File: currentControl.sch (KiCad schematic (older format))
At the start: 5 parts

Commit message: updated with association labels
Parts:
- gave numbers to parts that had none: 5
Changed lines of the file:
@@
 $EndDescr
 $Comp
-L GND #PWR?
+L GND #PWR205
 U 1 1 5521A09C
 P 5100 4750
-F 0 "#PWR?" H 5100 4500 60  0001 C CNN
+F 0 "#PWR205" H 5100 4500 60  0001 C CNN
 F 1 "GND" H 5100 4600 60  0000 C CNN
 F 2 "" H 5100 4750 60  0000 C CNN
@@
 $EndComp
 $Comp
-L GND #PWR?
+L GND #PWR201
 U 1 1 5521A0A9
 P 4300 3850
-F 0 "#PWR?" H 4300 3600 60  0001 C CNN
+F 0 "#PWR201" H 4300 3600 60  0001 C CNN
 F 1 "GND" H 4300 3700 60  0000 C CNN
 F 2 "" H 4300 3850 60  0000 C CNN
@@
 $EndComp
 $Comp
-L GND #PWR?
+L GND #PWR206
 U 1 1 5521A0D3
 P 5100 4750
-F 0 "#PWR?" H 5100 4500 60  0001 C CNN
+F 0 "#PWR206" H 5100 4500 60  0001 C CNN
 F 1 "GND" H 5100 4600 60  0000 C CNN
 F 2 "" H 5100 4750 60  0000 C CNN
@@
 $EndComp
 $Comp
-L GND #PWR?
+L GND #PWR202
 U 1 1 5521A0E0
 P 4300 3850
-F 0 "#PWR?" H 4300 3600 60  0001 C CNN
+F 0 "#PWR202" H 4300 3600 60  0001 C CNN
 F 1 "GND" H 4300 3700 60  0000 C CNN
 F 2 "" H 4300 3850 60  0000 C CNN
@@
 	7900 4450 7900 5200
 $Comp
-L GND #PWR?
+L GND #PWR207
 U 1 1 5521A118
 P 5100 4750
-F 0 "#PWR?" H 5100 4500 60  0001 C CNN
+F 0 "#PWR207" H 5100 4500 60  0001 C CNN
 F 1 "GND" H 5100 4600 60  0000 C CNN
 F 2 "" H 5100 4750 60  0000 C CNN
@@
 $EndComp
 $Comp
-L GND #PWR?
+L GND #PWR203
 U 1 1 5521A125
 P 4300 3850
-F 0 "#PWR?" H 4300 3600 60  0001 C CNN
+F 0 "#PWR203" H 4300 3600 60  0001 C CNN
 F 1 "GND" H 4300 3700 60  0000 C CNN
 F 2 "" H 4300 3850 60  0000 C CNN
@@
 $EndComp
 $Comp
-L LMV358 U?
+L LMV358 U201
 U 1 1 5521A12B
 P 5200 4250
-F 0 "U?" H 5150 4450 60  0000 L CNN
+F 0 "U201" H 5150 4450 60  0000 L CNN
 F 1 "LMV358" H 5150 4000 60  0000 L CNN
 F 2 "" H 5200 4250 60  0000 C CNN
@@
 $EndComp
 $Comp
-L R R?
+L R R202
 U 1 1 5521A139
 P 7900 5450
-F 0 "R?" V 7980 5450 50  0000 C CNN
+F 0 "R202" V 7980 5450 50  0000 C CNN
 F 1 ".1" V 7907 5451 50  0000 C CNN
 F 2 "" V 7830 5450 30  0000 C CNN
@@
 $EndComp
 $Comp
-L MOSFET_N Q?
+L MOSFET_N Q201
 U 1 1 5521A141
 P 7800 4250
-F 0 "Q?" H 7810 4420 50  0000 R CNN
+F 0 "Q201" H 7810 4420 50  0000 R CNN
 F 1 "BUK9575" H 7750 4100 50  0000 R CNN
 F 2 "" H 7800 4250 60  0000 C CNN
@@
 $EndComp
 $Comp
-L R R?
+L R R201
 U 1 1 5521A148
 P 6600 4250
-F 0 "R?" V 6680 4250 50  0000 C CNN
+F 0 "R201" V 6680 4250 50  0000 C CNN
 F 1 "R" V 6607 4251 50  0000 C CNN
 F 2 "" V 6530 4250 30  0000 C CNN
@@
 $EndComp
 $Comp
-L GND #PWR?
+L GND #PWR208
 U 1 1 5521A14F
 P 5100 4750
-F 0 "#PWR?" H 5100 4500 60  0001 C CNN
+F 0 "#PWR208" H 5100 4500 60  0001 C CNN
 F 1 "GND" H 5100 4600 60  0000 C CNN
 F 2 "" H 5100 4750 60  0000 C CNN
@@
 $EndComp
 $Comp
-L C C?
+L C C201
 U 1 1 5521A155
 P 4300 3550
-F 0 "C?" H 4350 3650 50  0000 L CNN
+F 0 "C201" H 4350 3650 50  0000 L CNN
 F 1 "C" H 4350 3450 50  0000 L CNN
 F 2 "" H 4338 3400 30  0000 C CNN
@@
 $EndComp
 $Comp
-L GND #PWR?
+L GND #PWR204
 U 1 1 5521A15C
 P 4300 3850
-F 0 "#PWR?" H 4300 3600 60  0001 C CNN
+F 0 "#PWR204" H 4300 3600 60  0001 C CNN
 F 1 "GND" H 4300 3700 60  0000 C CNN
 F 2 "" H 4300 3850 60  0000 C CNN

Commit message: updated schematic with corrected wiring after all passives became disconnected
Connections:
- wire segments 18 -> 19
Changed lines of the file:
@@
 	4700 4350 4700 5050
 Wire Wire Line
-	4300 3750 4300 3850
+	4300 3700 4300 3850
 Wire Wire Line
 	5100 4650 5100 4750
 Wire Wire Line
-	6850 4250 7600 4250
+	6750 4250 7600 4250
 Wire Wire Line
-	7900 4450 7900 5200
+	7900 4450 7900 5300
 $Comp
 L GND #PWR207
@@
 	2950 4150 4700 4150
 Wire Wire Line
-	5700 4250 6350 4250
+	5700 4250 6450 4250
 Wire Wire Line
 	7900 4050 7900 2000
@@
 Current_Sink-
 Wire Wire Line
-	7900 5700 7900 5800
+	7900 5600 7900 5800
 Wire Wire Line
 	7900 5800 8700 5800
+Wire Wire Line
+	4300 3400 4300 3350
+Connection ~ 4300 3350
 $EndSCHEMATC

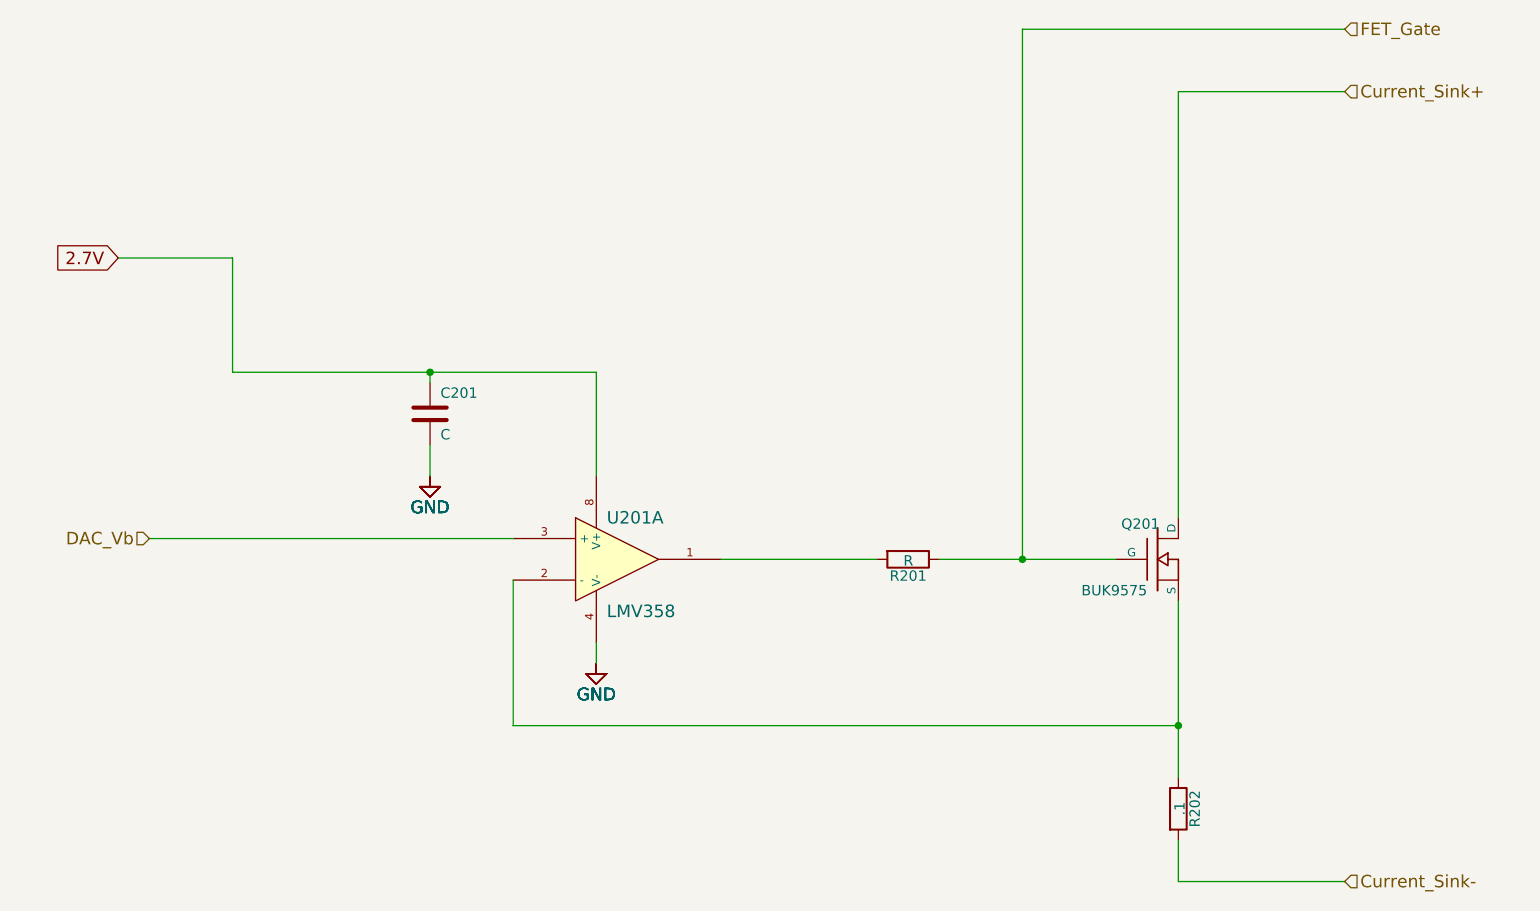
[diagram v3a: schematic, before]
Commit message: updated current control circuit with voltage divider to increase resolution to 12mA
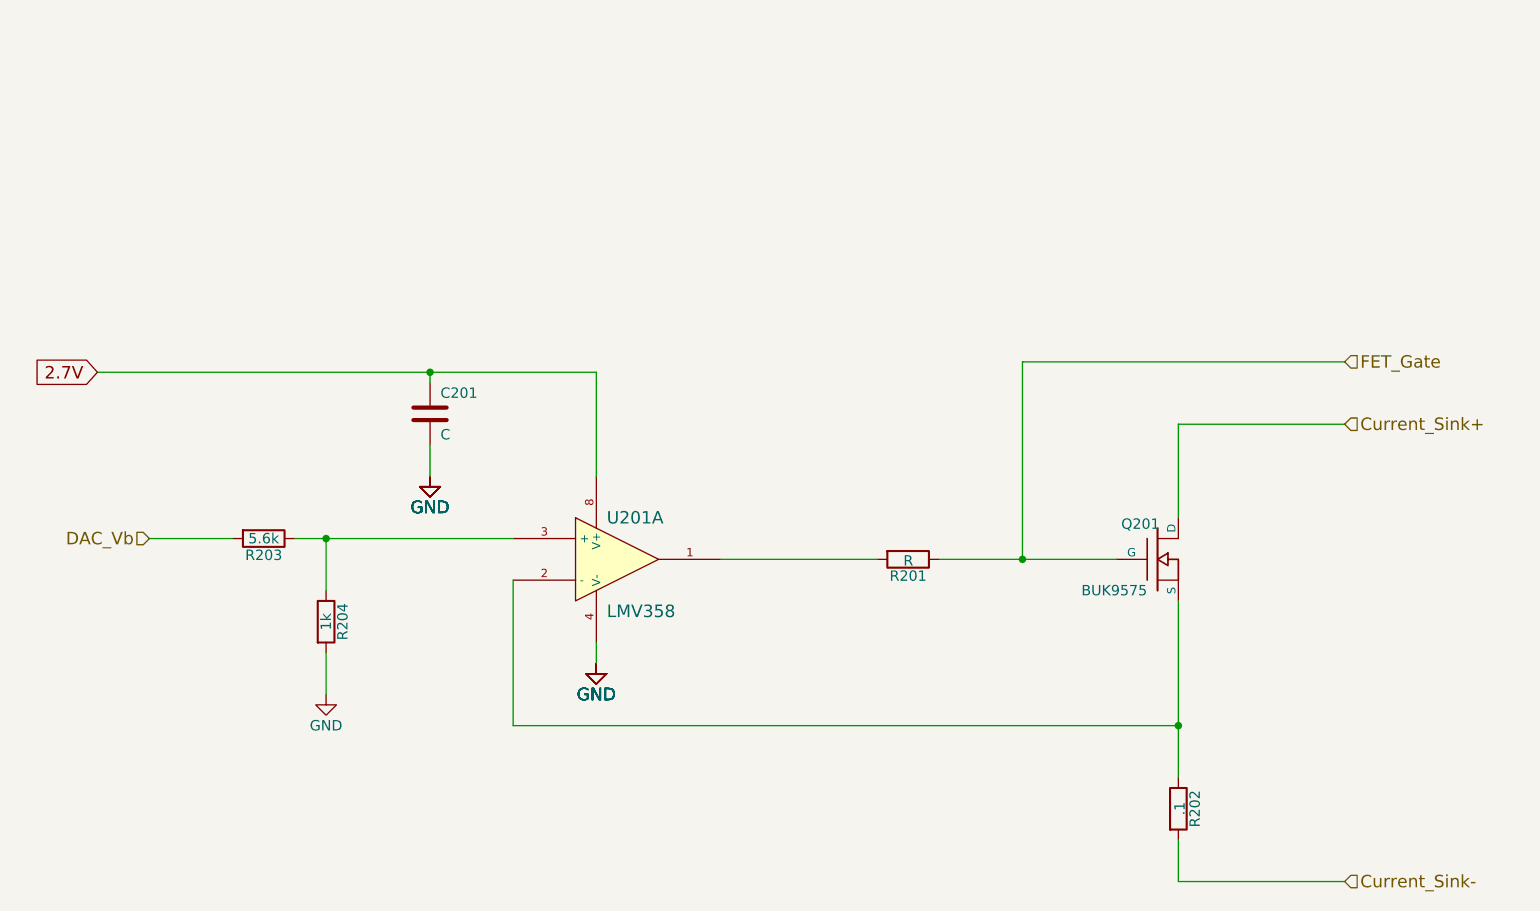
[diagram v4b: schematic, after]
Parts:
- added R203: 5.6k, symbol R
- added R204: 1k, symbol R
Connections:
- net DAC_Vb: now also R203.2; no longer U201.3 (+)
- net GND: now also R204.2
- new net: R203.1, R204.1, U201.3 (+)
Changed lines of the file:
@@
 $EndDescr
 $Comp
-L GND #PWR205
+L GND #PWR206
 U 1 1 5521A09C
 P 5100 4750
-F 0 "#PWR205" H 5100 4500 60  0001 C CNN
-F 1 "GND" H 5100 4600 60  0000 C CNN
-F 2 "" H 5100 4750 60  0000 C CNN
-F 3 "" H 5100 4750 60  0000 C CNN
-	1    5100 4750
-	1    0    0    -1
-$EndComp
-$Comp
-L GND #PWR201
+F 0 "#PWR206" H 5100 4500 60  0001 C CNN
+F 1 "GND" H 5100 4600 60  0000 C CNN
+F 2 "" H 5100 4750 60  0000 C CNN
+F 3 "" H 5100 4750 60  0000 C CNN
+	1    5100 4750
+	1    0    0    -1
+$EndComp
+$Comp
+L GND #PWR202
 U 1 1 5521A0A9
 P 4300 3850
-F 0 "#PWR201" H 4300 3600 60  0001 C CNN
-F 1 "GND" H 4300 3700 60  0000 C CNN
-F 2 "" H 4300 3850 60  0000 C CNN
-F 3 "" H 4300 3850 60  0000 C CNN
-	1    4300 3850
-	1    0    0    -1
-$EndComp
-$Comp
-L GND #PWR206
+F 0 "#PWR202" H 4300 3600 60  0001 C CNN
+F 1 "GND" H 4300 3700 60  0000 C CNN
+F 2 "" H 4300 3850 60  0000 C CNN
+F 3 "" H 4300 3850 60  0000 C CNN
+	1    4300 3850
+	1    0    0    -1
+$EndComp
+$Comp
+L GND #PWR207
 U 1 1 5521A0D3
 P 5100 4750
-F 0 "#PWR206" H 5100 4500 60  0001 C CNN
-F 1 "GND" H 5100 4600 60  0000 C CNN
-F 2 "" H 5100 4750 60  0000 C CNN
-F 3 "" H 5100 4750 60  0000 C CNN
-	1    5100 4750
-	1    0    0    -1
-$EndComp
-$Comp
-L GND #PWR202
+F 0 "#PWR207" H 5100 4500 60  0001 C CNN
+F 1 "GND" H 5100 4600 60  0000 C CNN
+F 2 "" H 5100 4750 60  0000 C CNN
+F 3 "" H 5100 4750 60  0000 C CNN
+	1    5100 4750
+	1    0    0    -1
+$EndComp
+$Comp
+L GND #PWR203
 U 1 1 5521A0E0
 P 4300 3850
-F 0 "#PWR202" H 4300 3600 60  0001 C CNN
-F 1 "GND" H 4300 3700 60  0000 C CNN
-F 2 "" H 4300 3850 60  0000 C CNN
-F 3 "" H 4300 3850 60  0000 C CNN
-	1    4300 3850
-	1    0    0    -1
-$EndComp
-Connection ~ 7900 5050
-Wire Wire Line
-	4700 5050 7900 5050
-Wire Wire Line
-	4700 4350 4700 5050
-Wire Wire Line
-	4300 3700 4300 3850
-Wire Wire Line
-	5100 4650 5100 4750
-Wire Wire Line
-	6750 4250 7600 4250
-Wire Wire Line
-	7900 4450 7900 5300
-$Comp
-L GND #PWR207
+F 0 "#PWR203" H 4300 3600 60  0001 C CNN
+F 1 "GND" H 4300 3700 60  0000 C CNN
+F 2 "" H 4300 3850 60  0000 C CNN
+F 3 "" H 4300 3850 60  0000 C CNN
+	1    4300 3850
+	1    0    0    -1
+$EndComp
+$Comp
+L GND #PWR208
 U 1 1 5521A118
 P 5100 4750
-F 0 "#PWR207" H 5100 4500 60  0001 C CNN
-F 1 "GND" H 5100 4600 60  0000 C CNN
-F 2 "" H 5100 4750 60  0000 C CNN
-F 3 "" H 5100 4750 60  0000 C CNN
-	1    5100 4750
-	1    0    0    -1
-$EndComp
-$Comp
-L GND #PWR203
+F 0 "#PWR208" H 5100 4500 60  0001 C CNN
+F 1 "GND" H 5100 4600 60  0000 C CNN
+F 2 "" H 5100 4750 60  0000 C CNN
+F 3 "" H 5100 4750 60  0000 C CNN
+	1    5100 4750
+	1    0    0    -1
+$EndComp
+$Comp
+L GND #PWR204
 U 1 1 5521A125
 P 4300 3850
-F 0 "#PWR203" H 4300 3600 60  0001 C CNN
+F 0 "#PWR204" H 4300 3600 60  0001 C CNN
 F 1 "GND" H 4300 3700 60  0000 C CNN
 F 2 "" H 4300 3850 60  0000 C CNN
@@
 $EndComp
 $Comp
-L GND #PWR208
+L GND #PWR209
 U 1 1 5521A14F
 P 5100 4750
-F 0 "#PWR208" H 5100 4500 60  0001 C CNN
+F 0 "#PWR209" H 5100 4500 60  0001 C CNN
 F 1 "GND" H 5100 4600 60  0000 C CNN
 F 2 "" H 5100 4750 60  0000 C CNN
@@
 $EndComp
 $Comp
-L GND #PWR204
+L GND #PWR205
 U 1 1 5521A15C
 P 4300 3850
-F 0 "#PWR204" H 4300 3600 60  0001 C CNN
-F 1 "GND" H 4300 3700 60  0000 C CNN
-F 2 "" H 4300 3850 60  0000 C CNN
-F 3 "" H 4300 3850 60  0000 C CNN
-	1    4300 3850
-	1    0    0    -1
-$EndComp
-Text GLabel 2800 2800 0    60   Input ~ 0
+F 0 "#PWR205" H 4300 3600 60  0001 C CNN
+F 1 "GND" H 4300 3700 60  0000 C CNN
+F 2 "" H 4300 3850 60  0000 C CNN
+F 3 "" H 4300 3850 60  0000 C CNN
+	1    4300 3850
+	1    0    0    -1
+$EndComp
+Text GLabel 2700 3350 0    60   Input ~ 0
 2.7V
-Wire Wire Line
-	5100 3850 5100 3350
-Wire Wire Line
-	5100 3350 3350 3350
-Wire Wire Line
-	3350 3350 3350 2800
-Wire Wire Line
-	3350 2800 2800 2800
 Text HLabel 2950 4150 0    60   Input ~ 0
 DAC_Vb
-Wire Wire Line
-	2950 4150 4700 4150
-Wire Wire Line
-	5700 4250 6450 4250
-Wire Wire Line
-	7900 4050 7900 2000
-Wire Wire Line
-	7900 2000 8700 2000
-Wire Wire Line
-	7150 4250 7150 1700
-Wire Wire Line
-	7150 1700 8700 1700
-Connection ~ 7150 4250
-Text HLabel 8700 1700 2    60   Input ~ 0
+Text HLabel 8700 3300 2    60   Input ~ 0
 FET_Gate
-Text HLabel 8700 2000 2    60   Input ~ 0
+Text HLabel 8700 3600 2    60   Input ~ 0
 Current_Sink+
 Text HLabel 8700 5800 2    60   Input ~ 0
 Current_Sink-
+$Comp
+L R R203
+U 1 1 5526E1C4
+P 3500 4150
+F 0 "R203" V 3580 4150 50  0000 C CNN
+F 1 "5.6k" V 3500 4150 50  0000 C CNN
+F 2 "" V 3430 4150 30  0000 C CNN
+F 3 "" H 3500 4150 30  0000 C CNN
+F 4 "Value" H 3500 4150 60  0001 C CNN "MPN"
+	1    3500 4150
+	0    1    1    0
+$EndComp
+$Comp
+L R R204
+U 1 1 5526E274
+P 3800 4550
+F 0 "R204" V 3880 4550 50  0000 C CNN
+F 1 "1k" V 3800 4550 50  0000 C CNN
+F 2 "" V 3730 4550 30  0000 C CNN
+F 3 "" H 3800 4550 30  0000 C CNN
+F 4 "Value" H 3800 4550 60  0001 C CNN "MPN"
+	1    3800 4550
+	1    0    0    -1
+$EndComp
+Connection ~ 7900 5050
+Wire Wire Line
+	4700 5050 7900 5050
+Wire Wire Line
+	4700 4350 4700 5050
+Wire Wire Line
+	4300 3700 4300 3850
+Wire Wire Line
+	5100 4650 5100 4750
+Wire Wire Line
+	6750 4250 7600 4250
+Wire Wire Line
+	7900 4450 7900 5300
+Wire Wire Line
+	5100 3350 5100 3850
+Wire Wire Line
+	2700 3350 5100 3350
+Wire Wire Line
+	5700 4250 6450 4250
+Wire Wire Line
+	7900 3600 8700 3600
+Connection ~ 7150 4250
 Wire Wire Line
 	7900 5600 7900 5800
@@
 	4300 3400 4300 3350
 Connection ~ 4300 3350
+Wire Wire Line
+	2950 4150 3350 4150
+Wire Wire Line
+	3650 4150 4700 4150
+Wire Wire Line
+	3800 4400 3800 4150
+Connection ~ 3800 4150
+$Comp
+L GND #PWR201
+U 1 1 5526E331
+P 3800 4900
+F 0 "#PWR201" H 3800 4650 50  0001 C CNN
+F 1 "GND" H 3800 4750 50  0000 C CNN
+F 2 "" H 3800 4900 60  0000 C CNN
+F 3 "" H 3800 4900 60  0000 C CNN
+	1    3800 4900
+	1    0    0    -1
+$EndComp
+Wire Wire Line
+	3800 4700 3800 4900
+Wire Wire Line
+	7150 3300 8700 3300
+Wire Wire Line
+	7900 3600 7900 4050
+Wire Wire Line
+	7150 3300 7150 4250
 $EndSCHEMATC

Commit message: updated project with most footprint associations
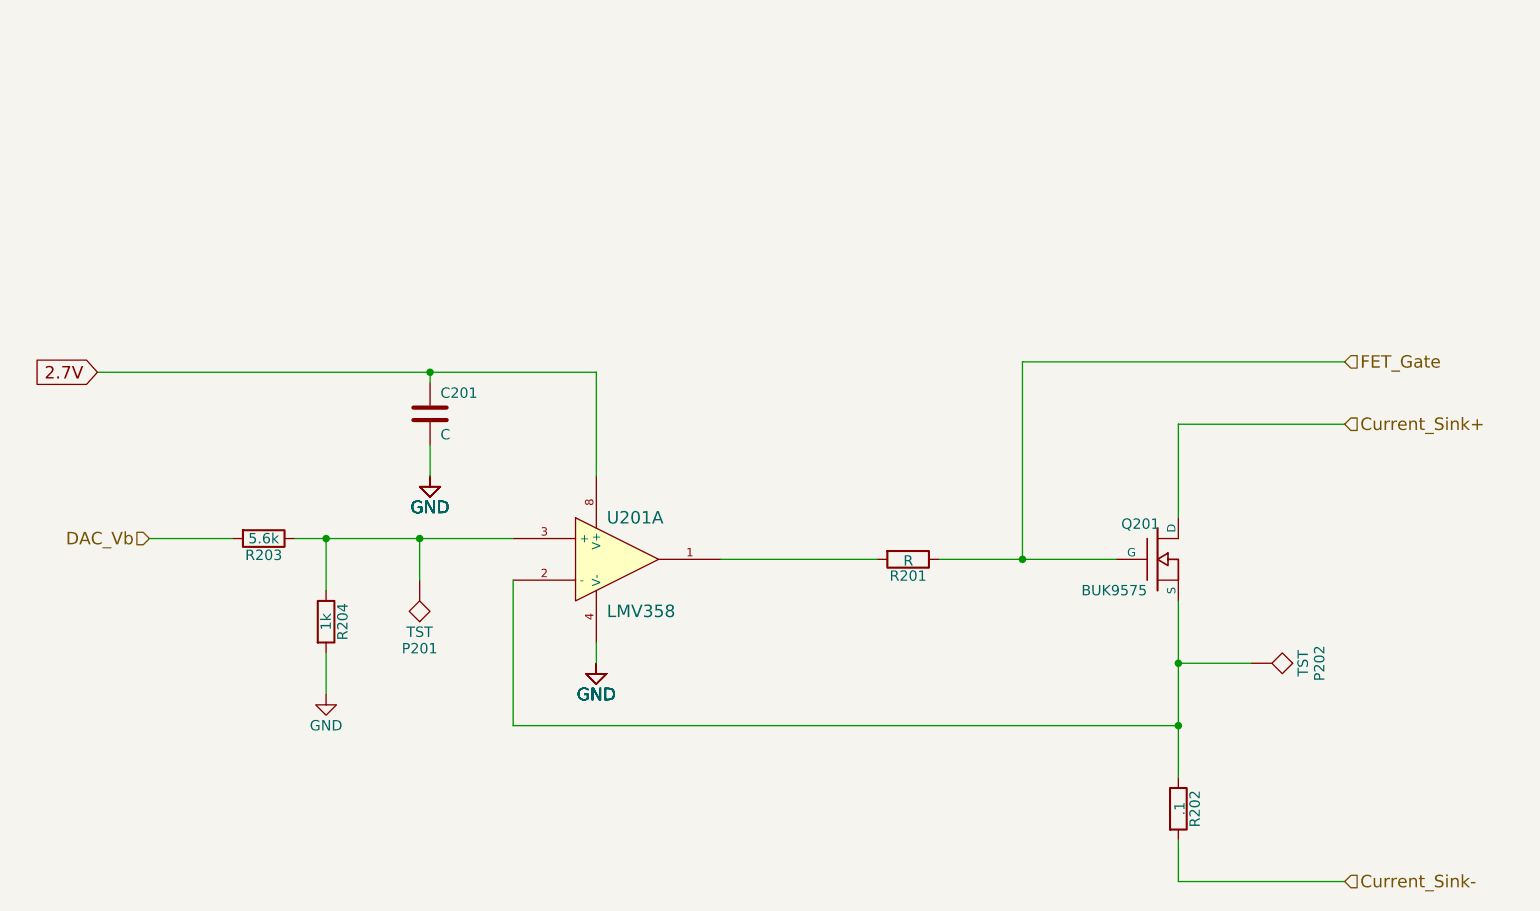
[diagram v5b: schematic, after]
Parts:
- added P201, P202: TST, symbol TST
- C201: footprint (none) -> Capacitors_SMD:C_0805_HandSoldering
- R201, R203, R204: footprint (none) -> Resistors_SMD:R_0805_HandSoldering
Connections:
- net at Q201.S, R202.1, U201.2 (-): now also P202.1
- net at R203.1, R204.1, U201.3 (+): now also P201.1
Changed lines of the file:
@@
 F 0 "U201" H 5150 4450 60  0000 L CNN
 F 1 "LMV358" H 5150 4000 60  0000 L CNN
-F 2 "" H 5200 4250 60  0000 C CNN
+F 2 "" H 5200 4250 60  0001 C CNN
 F 3 "" H 5200 4250 60  0000 C CNN
 	1    5200 4250
@@
 F 0 "R202" V 7980 5450 50  0000 C CNN
 F 1 ".1" V 7907 5451 50  0000 C CNN
-F 2 "" V 7830 5450 30  0000 C CNN
+F 2 "" V 7830 5450 30  0001 C CNN
 F 3 "" H 7900 5450 30  0000 C CNN
 F 4 "AC01000001007JA100" V 7900 5450 60  0001 C CNN "MPN"
@@
 F 0 "Q201" H 7810 4420 50  0000 R CNN
 F 1 "BUK9575" H 7750 4100 50  0000 R CNN
-F 2 "" H 7800 4250 60  0000 C CNN
+F 2 "" H 7800 4250 60  0001 C CNN
 F 3 "" H 7800 4250 60  0000 C CNN
 F 4 "BUK9575-100A,127" H 7800 4250 60  0001 C CNN "MPN"
@@
 F 0 "R201" V 6680 4250 50  0000 C CNN
 F 1 "R" V 6607 4251 50  0000 C CNN
-F 2 "" V 6530 4250 30  0000 C CNN
+F 2 "Resistors_SMD:R_0805_HandSoldering" V 6530 4250 30  0001 C CNN
 F 3 "" H 6600 4250 30  0000 C CNN
 	1    6600 4250
@@
 F 0 "C201" H 4350 3650 50  0000 L CNN
 F 1 "C" H 4350 3450 50  0000 L CNN
-F 2 "" H 4338 3400 30  0000 C CNN
+F 2 "Capacitors_SMD:C_0805_HandSoldering" H 4338 3400 30  0001 C CNN
 F 3 "" H 4300 3550 60  0000 C CNN
 	1    4300 3550
@@
 F 0 "R203" V 3580 4150 50  0000 C CNN
 F 1 "5.6k" V 3500 4150 50  0000 C CNN
-F 2 "" V 3430 4150 30  0000 C CNN
+F 2 "Resistors_SMD:R_0805_HandSoldering" V 3430 4150 30  0001 C CNN
 F 3 "" H 3500 4150 30  0000 C CNN
 F 4 "Value" H 3500 4150 60  0001 C CNN "MPN"
@@
 F 0 "R204" V 3880 4550 50  0000 C CNN
 F 1 "1k" V 3800 4550 50  0000 C CNN
-F 2 "" V 3730 4550 30  0000 C CNN
+F 2 "Resistors_SMD:R_0805_HandSoldering" V 3730 4550 30  0001 C CNN
 F 3 "" H 3800 4550 30  0000 C CNN
 F 4 "Value" H 3800 4550 60  0001 C CNN "MPN"
@@
 Wire Wire Line
 	7150 3300 7150 4250
+$Comp
+L TST P201
+U 1 1 5528EEEC
+P 4250 4350
+F 0 "P201" H 4250 4650 50  0000 C BNN
+F 1 "TST" H 4250 4600 50  0000 C CNN
+F 2 "" H 4250 4350 60  0000 C CNN
+F 3 "" H 4250 4350 60  0000 C CNN
+	1    4250 4350
+	-1   0    0    1
+$EndComp
+Wire Wire Line
+	4250 4350 4250 4150
+Connection ~ 4250 4150
+$Comp
+L TST P202
+U 1 1 5528F2F1
+P 8250 4750
+F 0 "P202" H 8250 5050 50  0000 C BNN
+F 1 "TST" H 8250 5000 50  0000 C CNN
+F 2 "" H 8250 4750 60  0000 C CNN
+F 3 "" H 8250 4750 60  0000 C CNN
+	1    8250 4750
+	0    1    1    0
+$EndComp
+Wire Wire Line
+	8250 4750 7900 4750
+Connection ~ 7900 4750
 $EndSCHEMATC
